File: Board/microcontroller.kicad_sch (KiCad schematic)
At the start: 23 parts, among them J9 ICSP, U2 PIC18F2480-ISO, Y1 10 MHz

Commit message: Bugfixes
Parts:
- D6: value RED -> DCHG
- D7: value GREEN -> CHG
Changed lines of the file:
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@@
 			)
 		)
-		(property "Value" "RED"
+		(property "Value" "DCHG"
 			(at 55.0672 108.0008 90)
 			(effects
@@
 			)
 		)
-		(property "Value" "GREEN"
+		(property "Value" "CHG"
 			(at 65.2272 108.0008 90)
 			(effects

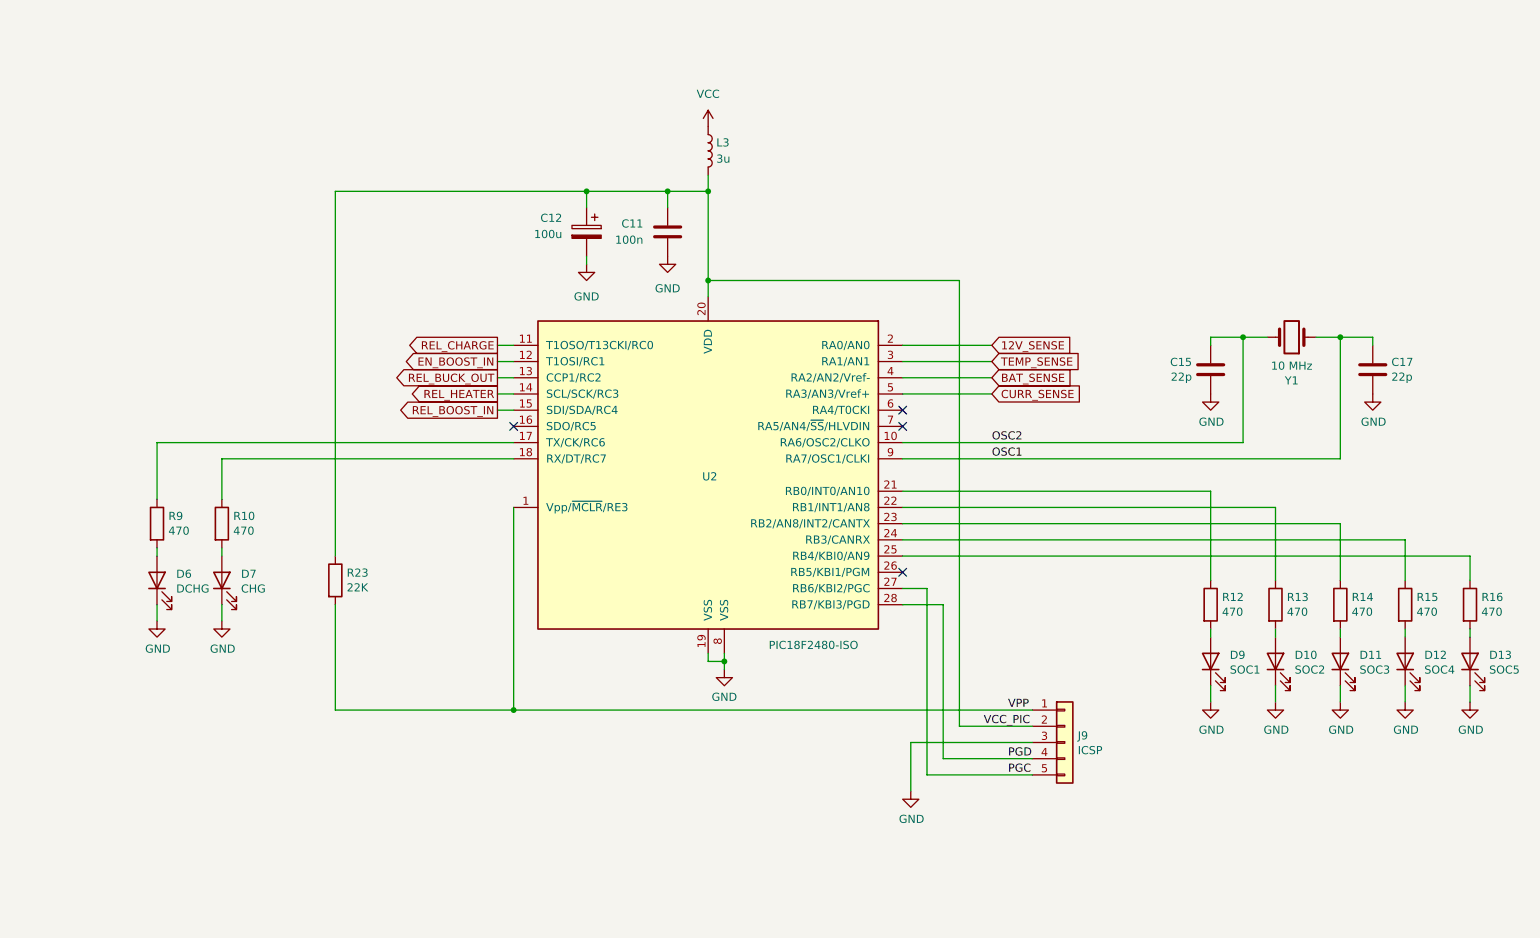
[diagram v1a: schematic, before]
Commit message: Set version number to 1.2. Various fixes. Add fan connector.
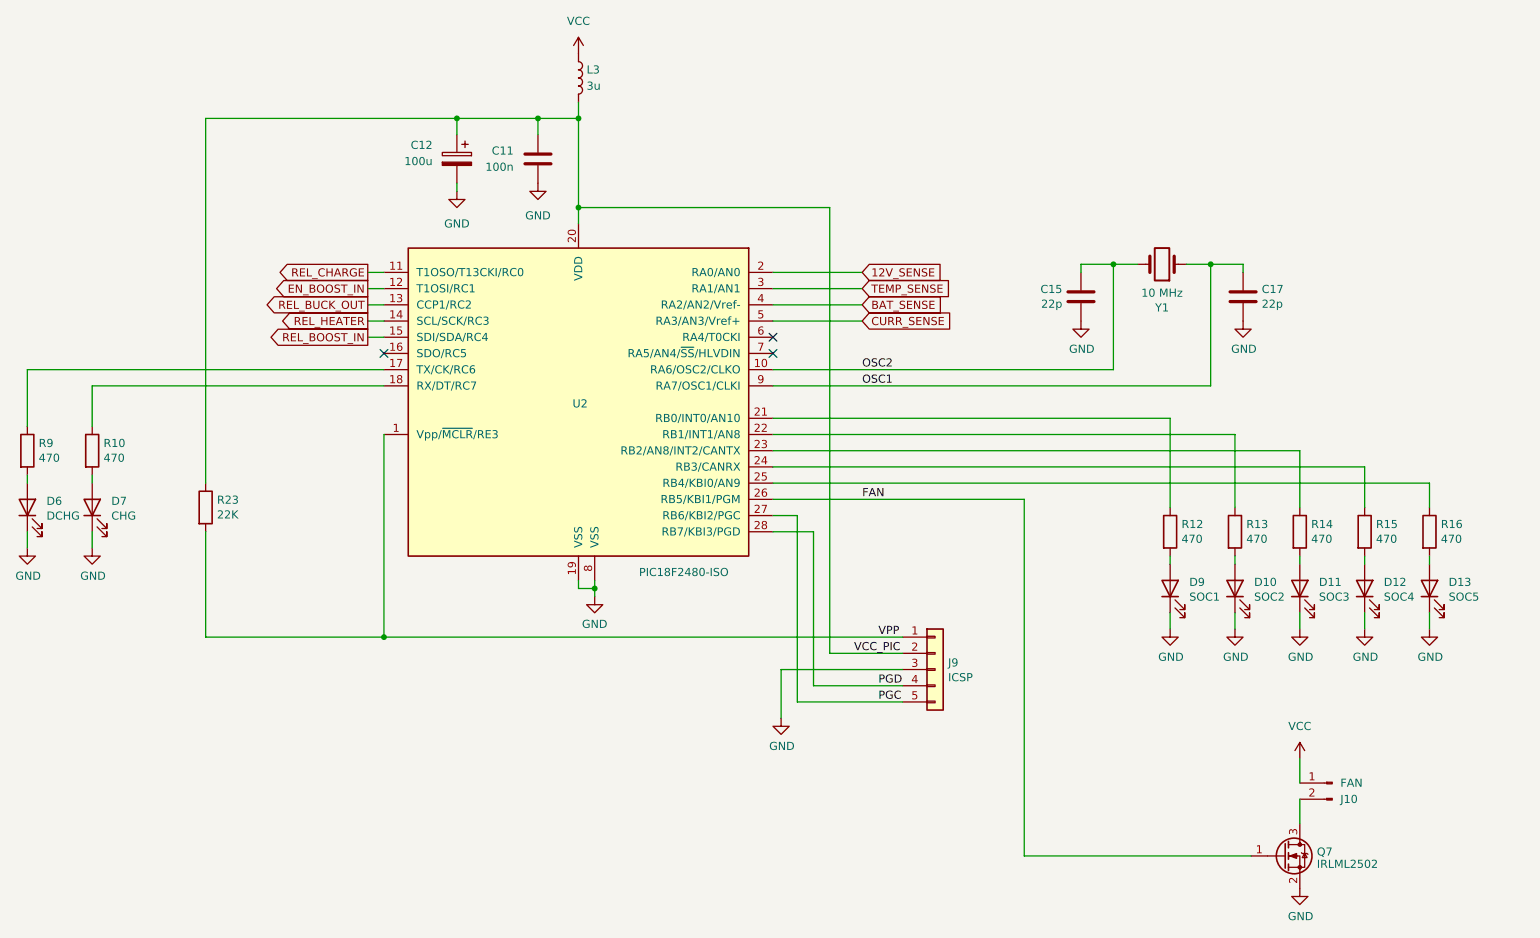
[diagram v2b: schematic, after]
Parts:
- added J10: FAN, Connector_JST:JST_PH_B2B-PH-K_1x02_P2.00mm_Vertical, symbol Connector:Conn_01x02_Pin
- added Q7: IRLML2502, Package_TO_SOT_SMD:SOT-23, symbol Transistor_FET:BSS138
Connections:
- net GND: now also Q7.2 (S)
- net VCC: now also J10.1 (Pin_1)
- net FAN: now reaches U2.26 (RB5/KBI1/PGM)
- net FAN: now also Q7.1 (G)
- new net: J10.2 (Pin_2), Q7.3 (D)
- no-connect marks 4 -> 3
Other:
- moved on the sheet: C11, C12, C15, C17, D10, D11, D12, D13, D6, D7, D9, J9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

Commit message: Adds connector for external duo LED
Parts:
- added J11: DUO LED, Connector_JST:JST_PH_B3B-PH-K_1x03_P2.00mm_Vertical, symbol Connector:Conn_01x03_Pin
- added R22, R25: 470, Resistor_SMD:R_0805_2012Metric, symbol Device:R
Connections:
- net GND: now also J11.2 (Pin_2)
- net at R10.1, U2.18 (RX/DT/RC7): now also R25.2
- net at R9.1, U2.17 (TX/CK/RC6): now also R22.2
- new net: J11.3 (Pin_3), R22.1
- new net: J11.1 (Pin_1), R25.1

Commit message: Bugfixes
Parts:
- added R26: 4K7, Resistor_SMD:R_0805_2012Metric, symbol Device:R
- added SW1: CALIBRATE, Button_Switch_SMD:SW_SPST_CK_RS282G05A3, symbol Switch:SW_Push
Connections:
- net GND: now also SW1.2
- net VCC_PIC: now also R26.1
- net CAL: now reaches U2.6 (RA4/T0CKI)
- net CAL: now also R26.2, SW1.1
- no-connect marks 3 -> 2

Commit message: Change fan connector.
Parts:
- J10: footprint Connector_JST:JST_PH_B2B-PH-K_1x02_P2.00mm_Vertical -> Connector_JST:JST_XH_B2B-XH-A_1x02_P2.50mm_Vertical
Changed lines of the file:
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@@
 			)
 		)
-		(property "Footprint" "Connector_JST:JST_PH_B2B-PH-K_1x02_P2.00mm_Vertical"
+		(property "Footprint" "Connector_JST:JST_XH_B2B-XH-A_1x02_P2.50mm_Vertical"
 			(at 236.22 138.43 0)
 			(effects

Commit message: Bugfixes
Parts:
- added C18: 100u, Capacitor_THT:CP_Radial_D5.0mm_P2.50mm, symbol Device:C_Polarized
- C12: footprint Capacitor_THT:CP_Radial_D6.3mm_P2.50mm -> Capacitor_THT:CP_Radial_D5.0mm_P2.50mm
- L3: value 3u -> 10u
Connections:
- net GND: now also C18.2
- net VCC_PIC renamed VCC_MCU
- net VCC_MCU: now also C18.1
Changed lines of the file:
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@@
 	)
 	(junction
+		(at 86.36 34.29)
+		(diameter 0)
+		(color 0 0 0 0)
+	)
+	(junction
+		(at 59.69 34.29)
+		(diameter 0)
+		(color 0 0 0 0)
+	)
+	(junction
 		(at 41.91 76.2)
 		(diameter 0)
@@
 	(wire
 		(pts
+			(xy 86.36 34.29) (xy 99.06 34.29)
+		)
+		(stroke
+			(width 0)
+			(type default)
+		)
+	)
+	(wire
+		(pts
 			(xy 31.75 91.44) (xy 31.75 90.17)
 		)
@@
 	(wire
 		(pts
+			(xy 86.36 44.45) (xy 86.36 46.99)
+		)
+		(stroke
+			(width 0)
+			(type default)
+		)
+	)
+	(wire
+		(pts
 			(xy 241.3 95.25) (xy 241.3 88.9)
 		)
@@
 	(wire
 		(pts
+			(xy 86.36 34.29) (xy 86.36 36.83)
+		)
+		(stroke
+			(width 0)
+			(type default)
+		)
+	)
+	(wire
+		(pts
 			(xy 231.14 140.97) (xy 231.14 144.78)
 		)
@@
 	(wire
 		(pts
+			(xy 59.69 34.29) (xy 86.36 34.29)
+		)
+		(stroke
+			(width 0)
+			(type default)
+		)
+	)
+	(wire
+		(pts
 			(xy 168.91 115.57) (xy 87.63 115.57)
 		)
@@
 	(wire
 		(pts
-			(xy 59.69 34.29) (xy 99.06 34.29)
-		)
-		(stroke
-			(width 0)
-			(type default)
-		)
-	)
-	(wire
-		(pts
 			(xy 220.98 95.25) (xy 220.98 83.82)
 		)
@@
 	(wire
 		(pts
+			(xy 57.15 34.29) (xy 59.69 34.29)
+		)
+		(stroke
+			(width 0)
+			(type default)
+		)
+	)
+	(wire
+		(pts
 			(xy 148.59 66.04) (xy 162.56 66.04)
 		)
@@
 		)
 	)
-	(label "VCC_PIC"
-		(at 161.29 118.11 0)
-		(fields_autoplaced yes)
-		(effects
-			(font
-				(size 1.27 1.27)
-			)
-			(justify left bottom)
-		)
-	)
 	(label "PGC"
 		(at 165.1 125.73 0)
@@
 		)
 	)
+	(global_label "VCC_MCU"
+		(shape output)
+		(at 57.15 34.29 180)
+		(fields_autoplaced yes)
+		(effects
+			(font
+				(size 1.27 1.27)
+			)
+			(justify right)
+		)
+		(property "Intersheetrefs" "${INTERSHEET_REFS}"
+			(at 45.5167 34.29 0)
+			(effects
+				(font
+					(size 1.27 1.27)
+				)
+				(justify right)
+				(hide yes)
+			)
+		)
+	)
 	(global_label "EN_BOOST_IN"
 		(shape output)
@@
 			)
 		)
-		(property "Value" "3u"
+		(property "Value" "10u"
 			(at 119.38 29.2099 0)
 			(effects
@@
 			)
 		)
-		(property "Footprint" "Capacitor_THT:CP_Radial_D6.3mm_P2.50mm"
+		(property "Footprint" "Capacitor_THT:CP_Radial_D5.0mm_P2.50mm"
 			(at 98.0948 44.45 0)
 			(effects
@@
 	)
 	(symbol
+		(lib_id "Device:C_Polarized")
+		(at 86.36 40.64 0)
+		(mirror y)
+		(unit 1)
+		(exclude_from_sim no)
+		(in_bom yes)
+		(on_board yes)
+		(dnp no)
+		(property "Reference" "C18"
+			(at 82.55 38.4809 0)
+			(effects
+				(font
+					(size 1.27 1.27)
+				)
+				(justify left)
+			)
+		)
+		(property "Value" "100u"
+			(at 82.55 41.0209 0)
+			(effects
+				(font
+					(size 1.27 1.27)
+				)
+				(justify left)
+			)
+		)
+		(property "Footprint" "Capacitor_THT:CP_Radial_D5.0mm_P2.50mm"
+			(at 85.3948 44.45 0)
+			(effects
+				(font
+					(size 1.27 1.27)
+				)
+				(hide yes)
+			)
+		)
+		(property "Datasheet" "~"
+			(at 86.36 40.64 0)
+			(effects
+				(font
+					(size 1.27 1.27)
+				)
+				(hide yes)
+			)
+		)
+		(property "Description" "Polarized capacitor"
+			(at 86.36 40.64 0)
+			(effects
+				(font
+					(size 1.27 1.27)
+				)
+				(hide yes)
+			)
+		)
+		(pin "2"
+		)
+		(pin "1"
+		)
+		(instances
+			(project "12VSupport"
+				(path "/f0c44745-560b-4dea-806a-2541c74a511b/3945f109-57ed-41f6-8253-6d6ba9eb298d"
+					(reference "C18")
+					(unit 1)
+				)
+			)
+		)
+	)
+	(symbol
 		(lib_id "Device:LED")
 		(at 220.98 107.95 90)
@@
 					(unit 1)
 				)
+			)
+		)
+	)
+	(symbol
+		(lib_id "power:GND")
+		(at 86.36 46.99 0)
+		(unit 1)
+		(exclude_from_sim no)
+		(in_bom yes)
+		(on_board yes)
+		(dnp no)
+		(fields_autoplaced yes)
+		(property "Reference" "#PWR055"
+			(at 86.36 53.34 0)
+			(effects
+				(font
+					(size 1.27 1.27)
+				)
+				(hide yes)
+			)
+		)
+		(property "Value" "GND"
+			(at 86.36 52.07 0)
+			(effects
+				(font
+					(size 1.27 1.27)
+				)
+			)
+		)
+		(property "Footprint" ""
+			(at 86.36 46.99 0)
+			(effects
+				(font
+					(size 1.27 1.27)
+				)
+				(hide yes)
+			)
+		)
+		(property "Datasheet" ""
+			(at 86.36 46.99 0)
+			(effects
+				(font
+					(size 1.27 1.27)
+				)
+				(hide yes)
+			)
+		)
+		(property "Description" "Power symbol creates a global label with name \"GND\" , ground"
+			(at 86.36 46.99 0)
+			(effects
+				(font
+					(size 1.27 1.27)
+				)
+				(hide yes)
+			)
+		)
+		(pin "1"
+		)
+		(instances
+			(project "12VSupport"
+				(path "/f0c44745-560b-4dea-806a-2541c74a511b/3945f109-57ed-41f6-8253-6d6ba9eb298d"
+					(reference "#PWR055")
+					(unit 1)
+				)

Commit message: New layout
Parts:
- added C19: 1u, Capacitor_SMD:C_1206_3216Metric, symbol Device:C
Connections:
- net VCC: now also C19.1
- net at J10.2 (Pin_2), Q7.3 (D): now also C19.2
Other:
- moved on the sheet: J10
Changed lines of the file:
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@@
 	)
 	(junction
+		(at 231.14 142.24)
+		(diameter 0)
+		(color 0 0 0 0)
+	)
+	(junction
 		(at 217.17 57.15)
 		(diameter 0)
@@
 	)
 	(junction
+		(at 231.14 132.08)
+		(diameter 0)
+		(color 0 0 0 0)
+	)
+	(junction
 		(at 118.11 48.26)
 		(diameter 0)
@@
 	(wire
 		(pts
-			(xy 231.14 140.97) (xy 231.14 144.78)
+			(xy 231.14 138.43) (xy 231.14 142.24)
 		)
 		(stroke
@@
 	(wire
 		(pts
-			(xy 231.14 134.62) (xy 231.14 138.43)
+			(xy 231.14 129.54) (xy 231.14 132.08)
 		)
 		(stroke
@@
 	(wire
 		(pts
+			(xy 224.79 142.24) (xy 231.14 142.24)
+		)
+		(stroke
+			(width 0)
+			(type default)
+		)
+	)
+	(wire
+		(pts
 			(xy 168.91 120.65) (xy 149.86 120.65)
 		)
@@
 	(wire
 		(pts
+			(xy 224.79 133.35) (xy 224.79 132.08)
+		)
+		(stroke
+			(width 0)
+			(type default)
+		)
+	)
+	(wire
+		(pts
 			(xy 217.17 57.15) (xy 217.17 76.2)
 		)
@@
 	(wire
 		(pts
+			(xy 231.14 132.08) (xy 231.14 135.89)
+		)
+		(stroke
+			(width 0)
+			(type default)
+		)
+	)
+	(wire
+		(pts
 			(xy 220.98 114.3) (xy 220.98 111.76)
 		)
@@
 	(wire
 		(pts
+			(xy 224.79 132.08) (xy 231.14 132.08)
+		)
+		(stroke
+			(width 0)
+			(type default)
+		)
+	)
+	(wire
+		(pts
 			(xy 31.75 54.61) (xy 34.29 54.61)
 		)
@@
 	(wire
 		(pts
+			(xy 224.79 140.97) (xy 224.79 142.24)
+		)
+		(stroke
+			(width 0)
+			(type default)
+		)
+	)
+	(wire
+		(pts
 			(xy 148.59 73.66) (xy 201.93 73.66)
 		)
@@
 	(wire
 		(pts
+			(xy 231.14 142.24) (xy 231.14 144.78)
+		)
+		(stroke
+			(width 0)
+			(type default)
+		)
+	)
+	(wire
+		(pts
 			(xy 36.83 50.8) (xy 36.83 52.07)
 		)
@@
 	)
 	(symbol
+		(lib_id "Device:C")
+		(at 224.79 137.16 0)
+		(mirror y)
+		(unit 1)
+		(exclude_from_sim no)
+		(in_bom yes)
+		(on_board yes)
+		(dnp no)
+		(property "Reference" "C19"
+			(at 221.869 135.9916 0)
+			(effects
+				(font
+					(size 1.27 1.27)
+				)
+				(justify left)
+			)
+		)
+		(property "Value" "1u"
+			(at 221.869 138.303 0)
+			(effects
+				(font
+					(size 1.27 1.27)
+				)
+				(justify left)
+			)
+		)
+		(property "Footprint" "Capacitor_SMD:C_1206_3216Metric"
+			(at 223.8248 140.97 0)
+			(effects
+				(font
+					(size 1.27 1.27)
+				)
+				(hide yes)
+			)
+		)
+		(property "Datasheet" "~"
+			(at 224.79 137.16 0)
+			(effects
+				(font
+					(size 1.27 1.27)
+				)
+				(hide yes)
+			)
+		)
+		(property "Description" ""
+			(at 224.79 137.16 0)
+			(effects
+				(font
+					(size 1.27 1.27)
+				)
+				(hide yes)
+			)
+		)
+		(pin "1"
+		)
+		(pin "2"
+		)
+		(instances
+			(project "12VSupport"
+				(path "/f0c44745-560b-4dea-806a-2541c74a511b/3945f109-57ed-41f6-8253-6d6ba9eb298d"
+					(reference "C19")
+					(unit 1)
+				)
+			)
+		)
+	)
+	(symbol
 		(lib_id "power:GND")
 		(at 41.91 101.6 0)
@@
 	(symbol
 		(lib_id "Connector:Conn_01x02_Pin")
-		(at 236.22 138.43 0)
+		(at 236.22 135.89 0)
 		(mirror y)
 		(unit 1)
@@
 		(dnp no)
 		(property "Reference" "J10"
-			(at 237.49 140.9701 0)
+			(at 237.49 138.4301 0)
 			(effects
 				(font
@@
 		)
 		(property "Value" "FAN"
-			(at 237.49 138.4301 0)
+			(at 237.49 135.8901 0)
 			(effects
 				(font
@@
 		)
 		(property "Footprint" "Connector_JST:JST_XH_B2B-XH-A_1x02_P2.50mm_Vertical"
-			(at 236.22 138.43 0)
+			(at 236.22 135.89 0)
 			(effects
 				(font
@@
 		)
 		(property "Datasheet" "~"
-			(at 236.22 138.43 0)
+			(at 236.22 135.89 0)
 			(effects
 				(font
@@
 		)
 		(property "Description" "Generic connector, single row, 01x02, script generated"
-			(at 236.22 138.43 0)
+			(at 236.22 135.89 0)
 			(effects
 				(font
@@
 	(symbol
 		(lib_id "power:VCC")
-		(at 231.14 134.62 0)
+		(at 231.14 129.54 0)
 		(unit 1)
 		(exclude_from_sim no)
@@
 		(fields_autoplaced yes)
 		(property "Reference" "#PWR040"
-			(at 231.14 138.43 0)
+			(at 231.14 133.35 0)
 			(effects
 				(font
@@
 		)
 		(property "Value" "VCC"
-			(at 231.14 129.54 0)
+			(at 231.14 124.46 0)
 			(effects
 				(font
@@
 		)
 		(property "Footprint" ""
-			(at 231.14 134.62 0)
+			(at 231.14 129.54 0)
 			(effects
 				(font
@@
 		)
 		(property "Datasheet" ""
-			(at 231.14 134.62 0)
+			(at 231.14 129.54 0)
 			(effects
 				(font
@@
 		)
 		(property "Description" "Power symbol creates a global label with name \"VCC\""
-			(at 231.14 134.62 0)
+			(at 231.14 129.54 0)
 			(effects
 				(font
